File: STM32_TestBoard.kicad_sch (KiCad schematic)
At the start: 0 parts

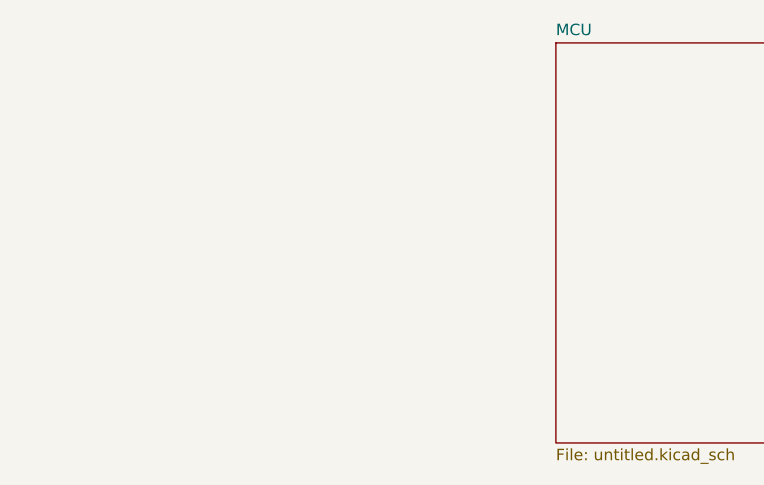
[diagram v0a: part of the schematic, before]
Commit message: Added differential lines and usb connect
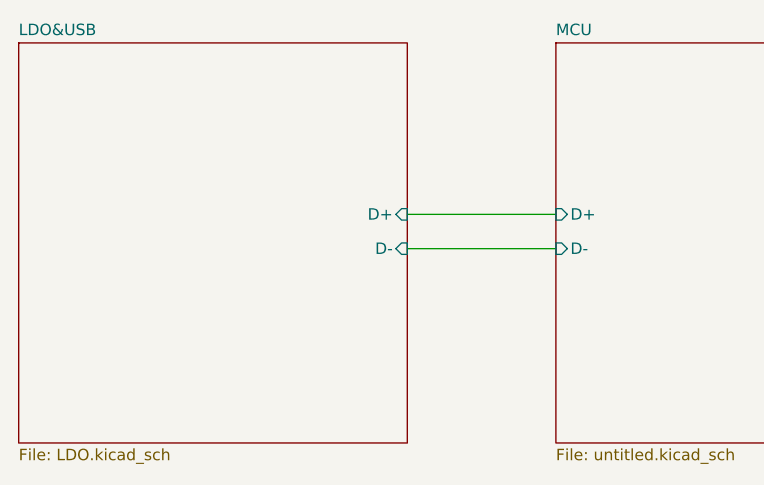
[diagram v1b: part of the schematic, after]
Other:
- added sheet LDO&USB (LDO.kicad_sch)
- sheet MCU ports: added D+, D-; removed none
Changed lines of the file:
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@@
 	(generator_version "9.0")
 	(paper "A4")
+	(wire
+		(pts
+			(xy 180.34 59.69) (xy 196.85 59.69)
+		)
+		(stroke
+			(width 0)
+			(type default)
+		)
+	)
+	(wire
+		(pts
+			(xy 180.34 55.88) (xy 196.85 55.88)
+		)
+		(stroke
+			(width 0)
+			(type default)
+		)
+	)
 	(sheet
 		(at 196.85 36.83)
@@
 			)
 		)
+		(pin "D+" input
+			(at 196.85 55.88 180)
+			(effects
+				(font
+					(size 1.27 1.27)
+				)
+				(justify left)
+			)
+		)
+		(pin "D-" input
+			(at 196.85 59.69 180)
+			(effects
+				(font
+					(size 1.27 1.27)
+				)
+				(justify left)
+			)
+		)
 		(instances
 			(project "STM32_TestBoard"
@@
 				)
 			)
+		)
+	)
+	(sheet
+		(at 137.16 36.83)
+		(size 43.18 44.45)
+		(exclude_from_sim no)
+		(in_bom yes)
+		(on_board yes)
+		(dnp no)
+		(fields_autoplaced yes)
+		(stroke
+			(width 0.1524)
+			(type solid)
+		)
+		(fill
+			(color 0 0 0 0.0000)
+		)
+		(property "Sheetname" "LDO&USB"
+			(at 137.16 36.1184 0)
+			(effects
+				(font
+					(size 1.27 1.27)
+				)
+				(justify left bottom)
+			)
+		)
+		(property "Sheetfile" "LDO.kicad_sch"
+			(at 137.16 81.8646 0)
+			(effects
+				(font
+					(size 1.27 1.27)
+				)
+				(justify left top)
+			)
+		)
+		(pin "D+" input
+			(at 180.34 55.88 0)
+			(effects
+				(font
+					(size 1.27 1.27)
+				)
+				(justify right)
+			)
+		)
+		(pin "D-" input
+			(at 180.34 59.69 0)
+			(effects
+				(font
+					(size 1.27 1.27)
+				)
+				(justify right)
+			)
+		)
+		(instances
+			(project "STM32_TestBoard"
+				(path "/18aebc4d-5de9-4f62-bc1c-f673cb616b21"
+					(page "3")
+				)
+			)

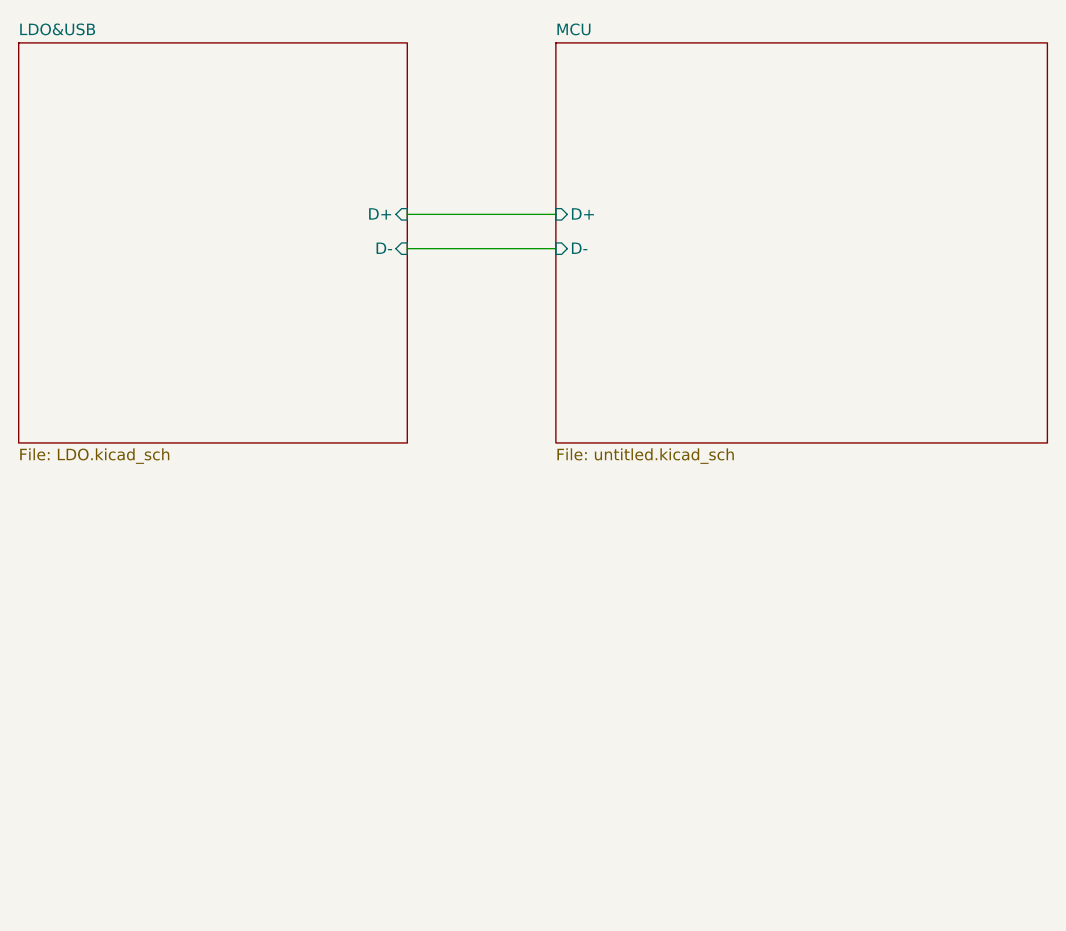
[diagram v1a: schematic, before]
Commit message: adding can IC
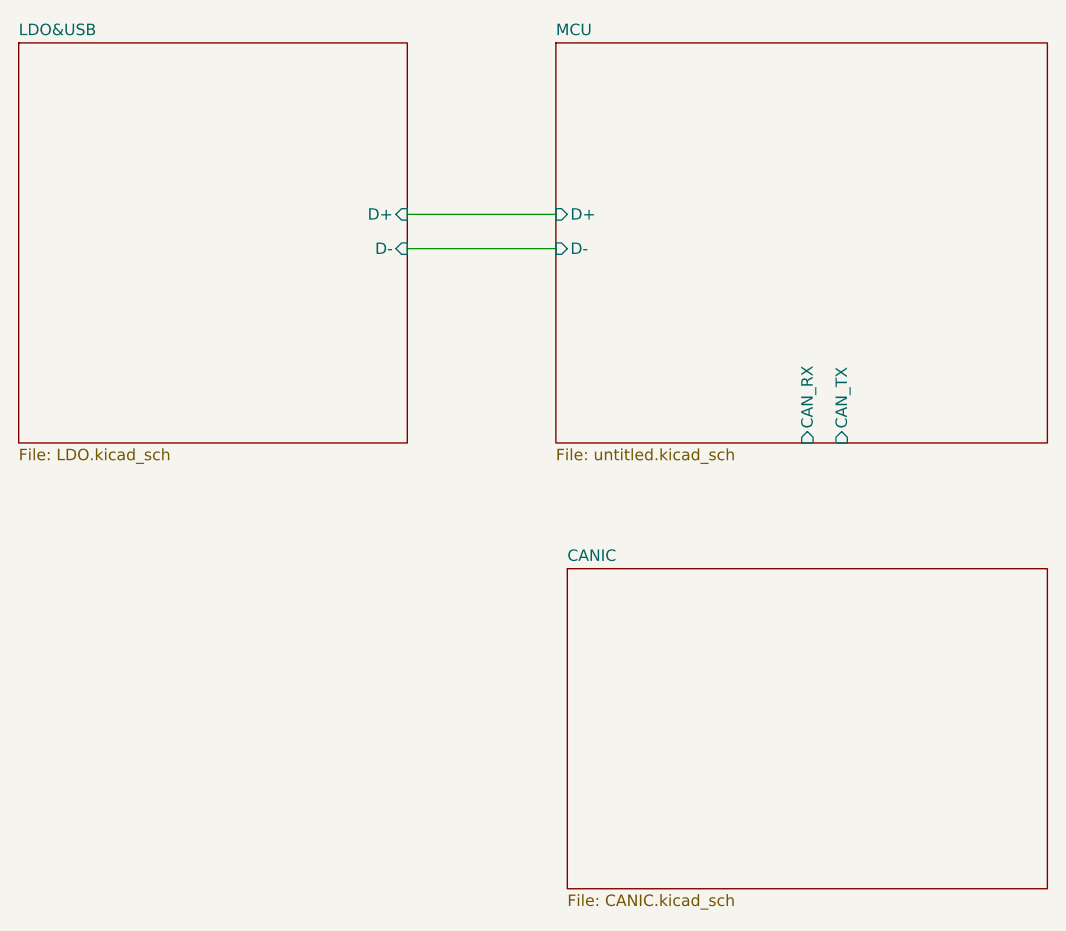
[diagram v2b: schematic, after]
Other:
- added sheet CANIC (CANIC.kicad_sch)
- sheet MCU ports: added CAN_RX, CAN_TX; removed none
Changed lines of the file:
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@@
 (kicad_sch
-	(version 20250114)
+	(version 20260306)
 	(generator "eeschema")
-	(generator_version "9.0")
+	(generator_version "10.0")
 	(paper "A4")
 	(wire
@@
 		)
 		(fill
-			(color 0 0 0 0.0000)
+			(color 0 0 0 0)
 		)
 		(property "Sheetname" "MCU"
 			(at 196.85 36.1184 0)
+			(show_name no)
+			(do_not_autoplace no)
 			(effects
 				(font
@@
 		(property "Sheetfile" "untitled.kicad_sch"
 			(at 196.85 81.8646 0)
+			(show_name no)
+			(do_not_autoplace no)
 			(effects
 				(font
@@
 		(pin "D-" input
 			(at 196.85 59.69 180)
+			(effects
+				(font
+					(size 1.27 1.27)
+				)
+				(justify left)
+			)
+		)
+		(pin "CAN_RX" input
+			(at 224.79 81.28 270)
+			(effects
+				(font
+					(size 1.27 1.27)
+				)
+				(justify left)
+			)
+		)
+		(pin "CAN_TX" input
+			(at 228.6 81.28 270)
 			(effects
 				(font
@@
 		)
 		(fill
-			(color 0 0 0 0.0000)
+			(color 0 0 0 0)
 		)
 		(property "Sheetname" "LDO&USB"
 			(at 137.16 36.1184 0)
+			(show_name no)
+			(do_not_autoplace no)
 			(effects
 				(font
@@
 		(property "Sheetfile" "LDO.kicad_sch"
 			(at 137.16 81.8646 0)
+			(show_name no)
+			(do_not_autoplace no)
 			(effects
 				(font
@@
 				)
 			)
+		)
+	)
+	(sheet
+		(at 198.12 95.25)
+		(size 53.34 35.56)
+		(exclude_from_sim no)
+		(in_bom yes)
+		(on_board yes)
+		(dnp no)
+		(fields_autoplaced yes)
+		(stroke
+			(width 0.1524)
+			(type solid)
+		)
+		(fill
+			(color 0 0 0 0)
+		)
+		(property "Sheetname" "CANIC"
+			(at 198.12 94.5384 0)
+			(show_name no)
+			(do_not_autoplace no)
+			(effects
+				(font
+					(size 1.27 1.27)
+				)
+				(justify left bottom)
+			)
+		)
+		(property "Sheetfile" "CANIC.kicad_sch"
+			(at 198.12 131.3946 0)
+			(show_name no)
+			(do_not_autoplace no)
+			(effects
+				(font
+					(size 1.27 1.27)
+				)
+				(justify left top)
+			)
+		)
+		(instances
+			(project "STM32_TestBoard"
+				(path "/18aebc4d-5de9-4f62-bc1c-f673cb616b21"
+					(page "4")
+				)
+			)
